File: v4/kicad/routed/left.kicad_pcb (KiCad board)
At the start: 2 copper layers, 158 x 119 mm, 68 parts

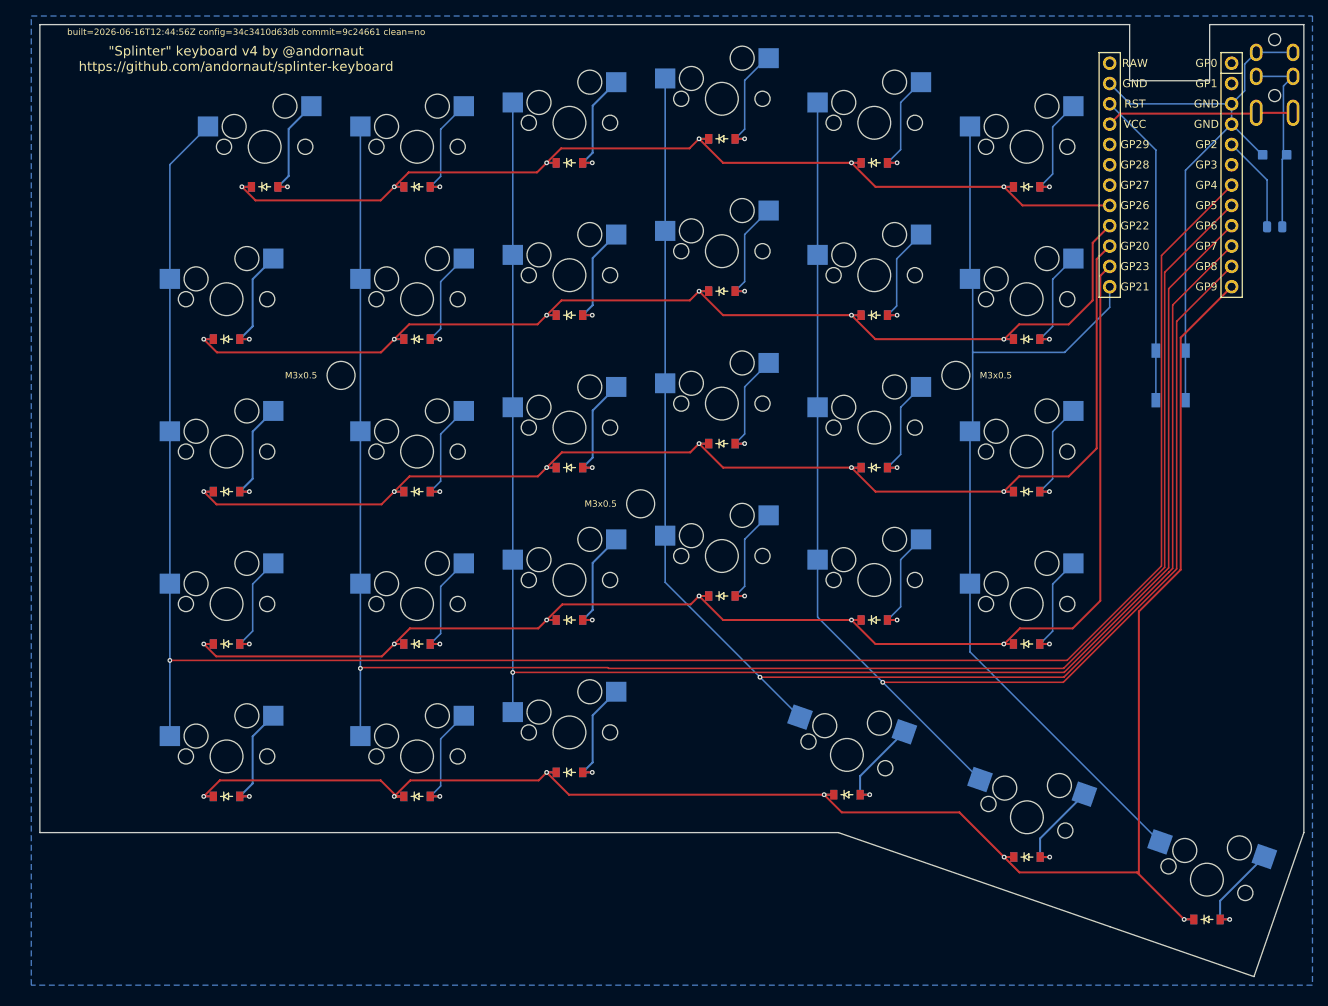
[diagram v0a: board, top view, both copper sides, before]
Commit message: v4: reassign left-half matrix pins, re-sync boards, harden GND guard
config.yaml: column five left -> P15 (was P10) and swap the lower/home/
upper row_net assignments (P14/P16/P10). Re-sync routed/ + unrouted/
left and right boards to the new config.

add-gnd-zone.py: exclude teardrop zones from the already-poured guard (a
teardrop on a GND track is itself a GND zone, which made the guard see a
pour that was never flooded and skip the real fill); clearer
UNCHANGED/ADDED logging.
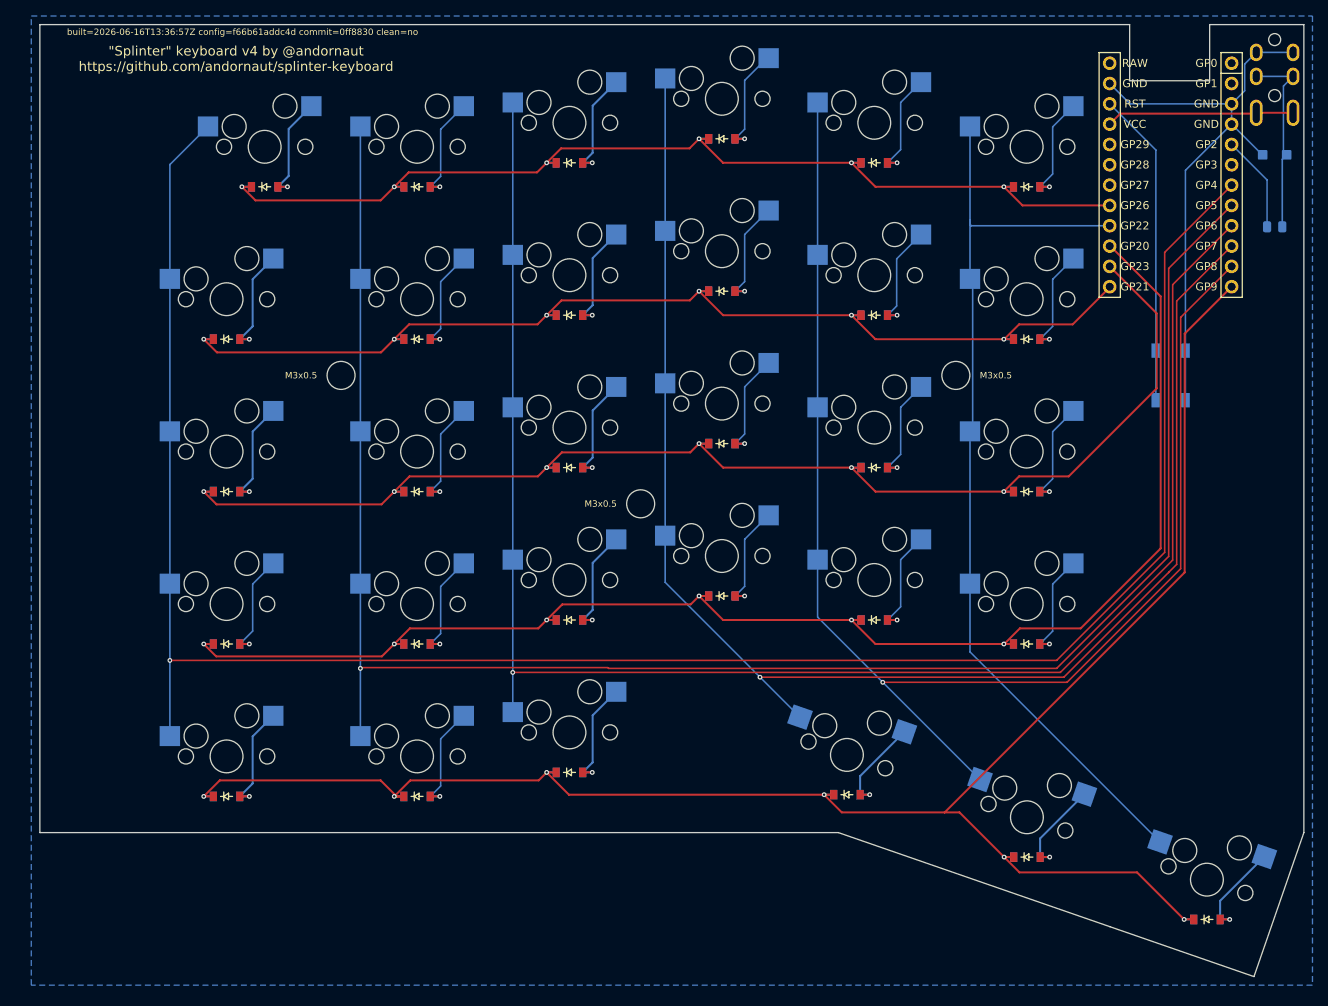
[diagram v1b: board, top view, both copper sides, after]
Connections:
- D12 pad 1: P16 -> P14
- D13 pad 1: P14 -> P16
- D14 pad 1: P15 -> P10
- D16 pad 1: P16 -> P14
- D17 pad 1: P14 -> P16
- D18 pad 1: P15 -> P10
- D2 pad 1: P16 -> P14
- D20 pad 1: P16 -> P14
- D21 pad 1: P14 -> P16
- D22 pad 1: P15 -> P10
- D24 pad 1: P16 -> P14
- D25 pad 1: P14 -> P16
- D26 pad 1: P15 -> P10
- D3 pad 1: P14 -> P16
- D4 pad 1: P15 -> P10
- D7 pad 1: P16 -> P14
- D8 pad 1: P14 -> P16
- D9 pad 1: P15 -> P10
- S24 pad 1: P10 -> P15
- S25 pad 1: P10 -> P15
- S26 pad 1: P10 -> P15
- S27 pad 1: P10 -> P15
- S30 pad 1: P10 -> P15
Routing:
- net P15: track 144.1 -> 116.6 mm, vias 6 -> 0
- net P14: track 160.5 -> 185.6 mm
- net P10: track 120.6 -> 136.7 mm, vias 0 -> 6
- net P16: track 177.2 -> 162.8 mm
- net P9: track 227.2 -> 229.5 mm
- net P4: track 258.2 -> 257.4 mm
- net P5: track 230.8 -> 230.2 mm
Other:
- board text added: "built=2026-06-16T13:36:57Z config=f66b61addc4d commit=0ff8830 clean=no"
- board text removed: "built=2026-06-16T12:44:56Z config=34c3410d63db commit=9c24661 clean=no"

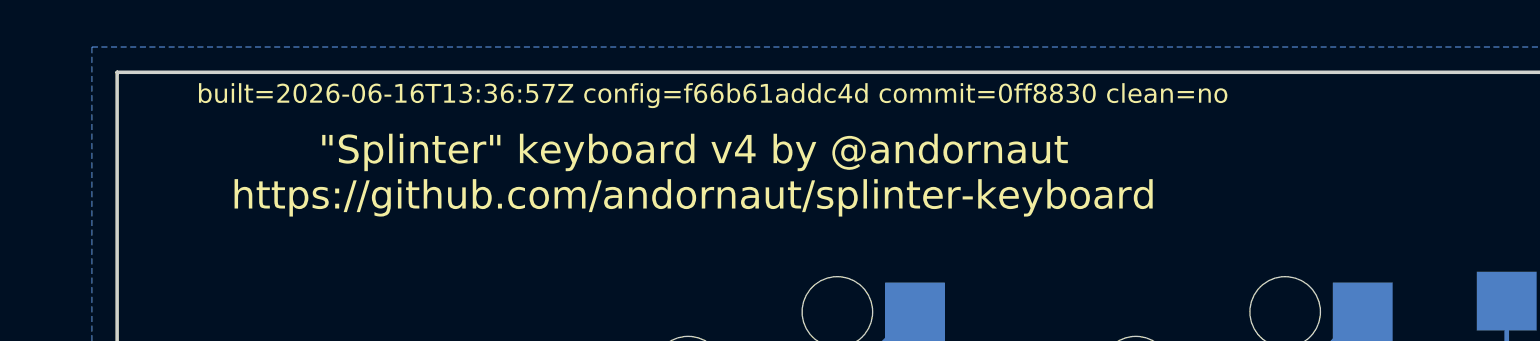
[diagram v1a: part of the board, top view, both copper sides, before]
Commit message: v4: regenerate boards with GND pour fix (JLCPCB order build)
Re-synced unrouted + routed left/right boards. This is the build sent to
JLCPCB: stamp built=2026-06-16T14:04:40Z config=f66b61addc4d commit=44bb610
clean=yes.
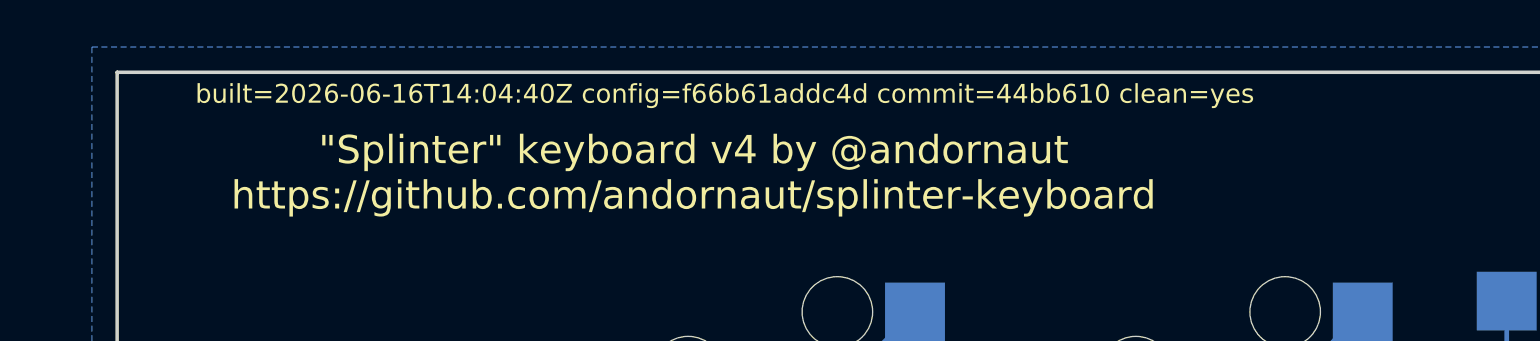
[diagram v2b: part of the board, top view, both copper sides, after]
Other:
- board text added: "built=2026-06-16T14:04:40Z config=f66b61addc4d commit=44bb610 clean=yes"
- board text removed: "built=2026-06-16T13:36:57Z config=f66b61addc4d commit=0ff8830 clean=no"

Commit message: v4: restore right-half teardrops on routed + unrouted masters
The right master carried only 20 teardrop zones (the teardrop-loss
failure that shipped on the first JLCPCB order); re-teardropped to 502,
now symmetric with the left half (464). Tracks, vias, and arcs are
unchanged on both halves (408/70/128 right, 384/65/120 left); the rest
of the diff is KiCad re-save churn. Clears the validate:fab
teardrop-consistency gate.
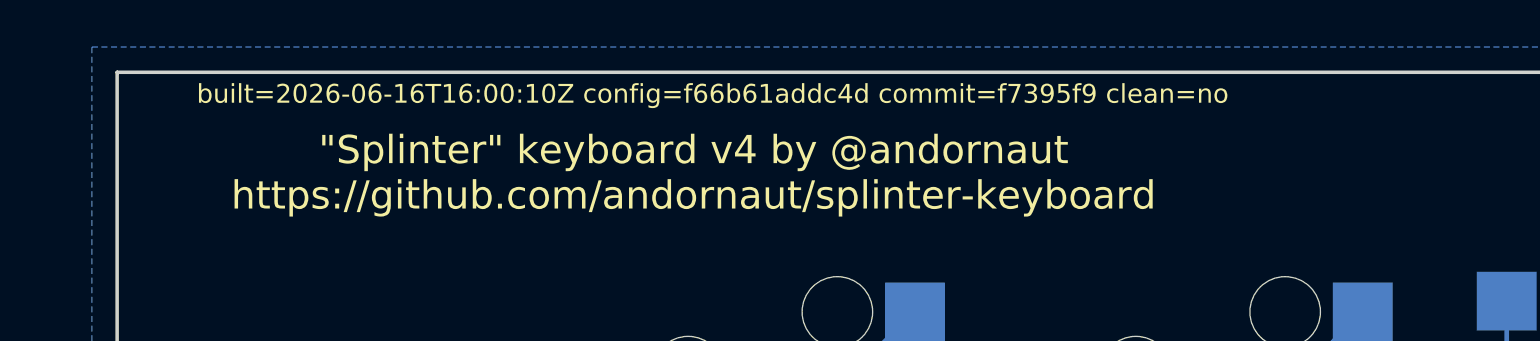
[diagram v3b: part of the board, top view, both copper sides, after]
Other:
- board text added: "built=2026-06-16T16:00:10Z config=f66b61addc4d commit=f7395f9 clean=no"
- board text removed: "built=2026-06-16T14:04:40Z config=f66b61addc4d commit=44bb610 clean=yes"

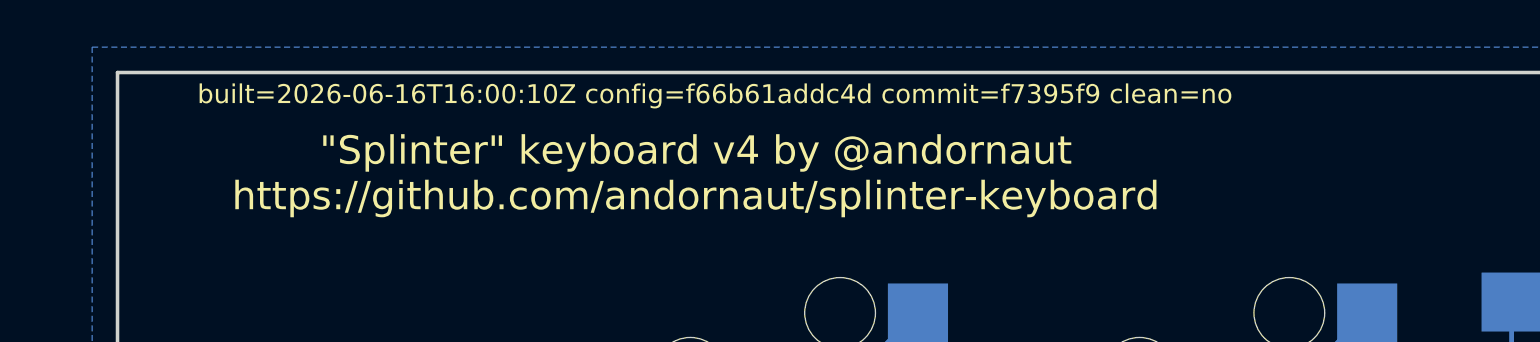
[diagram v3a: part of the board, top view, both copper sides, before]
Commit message: v4: fabrication build (ordering this from JLCPCB)
Validated fab-ready and sent to JLCPCB. Teardrops symmetric (459 left /
496 right zones), GND pour filled on B.Cu (~13000mm^2 master, ~157x118mm
flood in the shipped B_Cu gerber), DRC clean (0 violations / 0 unconnected
both halves), provenance matches config, gerber set + assembly complete.

Provenance stamp (routed masters):
  splinter v=v4 built=2026-06-16T16:30:02Z config=f66b61addc4d commit=d2fd01a clean=yes
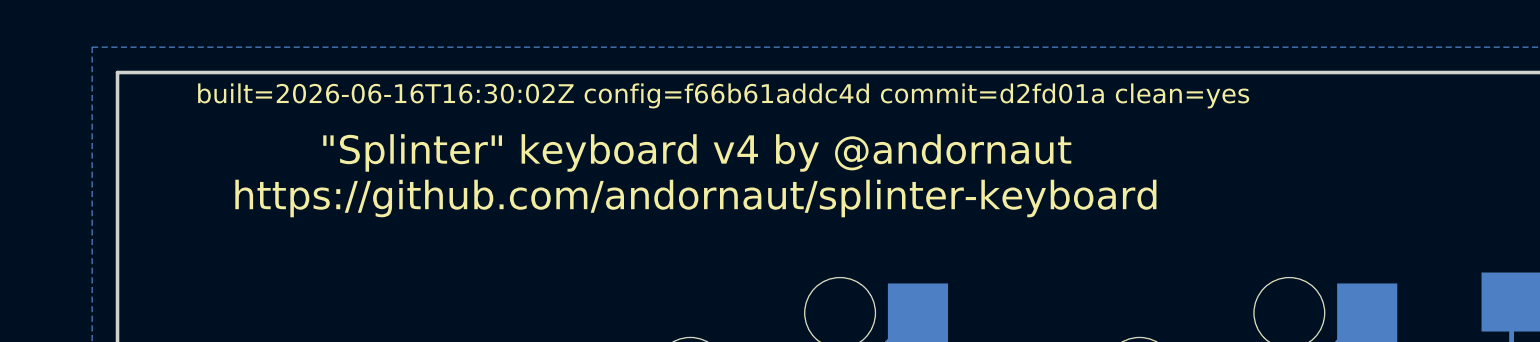
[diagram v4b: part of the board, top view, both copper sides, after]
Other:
- board text added: "built=2026-06-16T16:30:02Z config=f66b61addc4d commit=d2fd01a clean=yes"
- board text removed: "built=2026-06-16T16:00:10Z config=f66b61addc4d commit=f7395f9 clean=no"

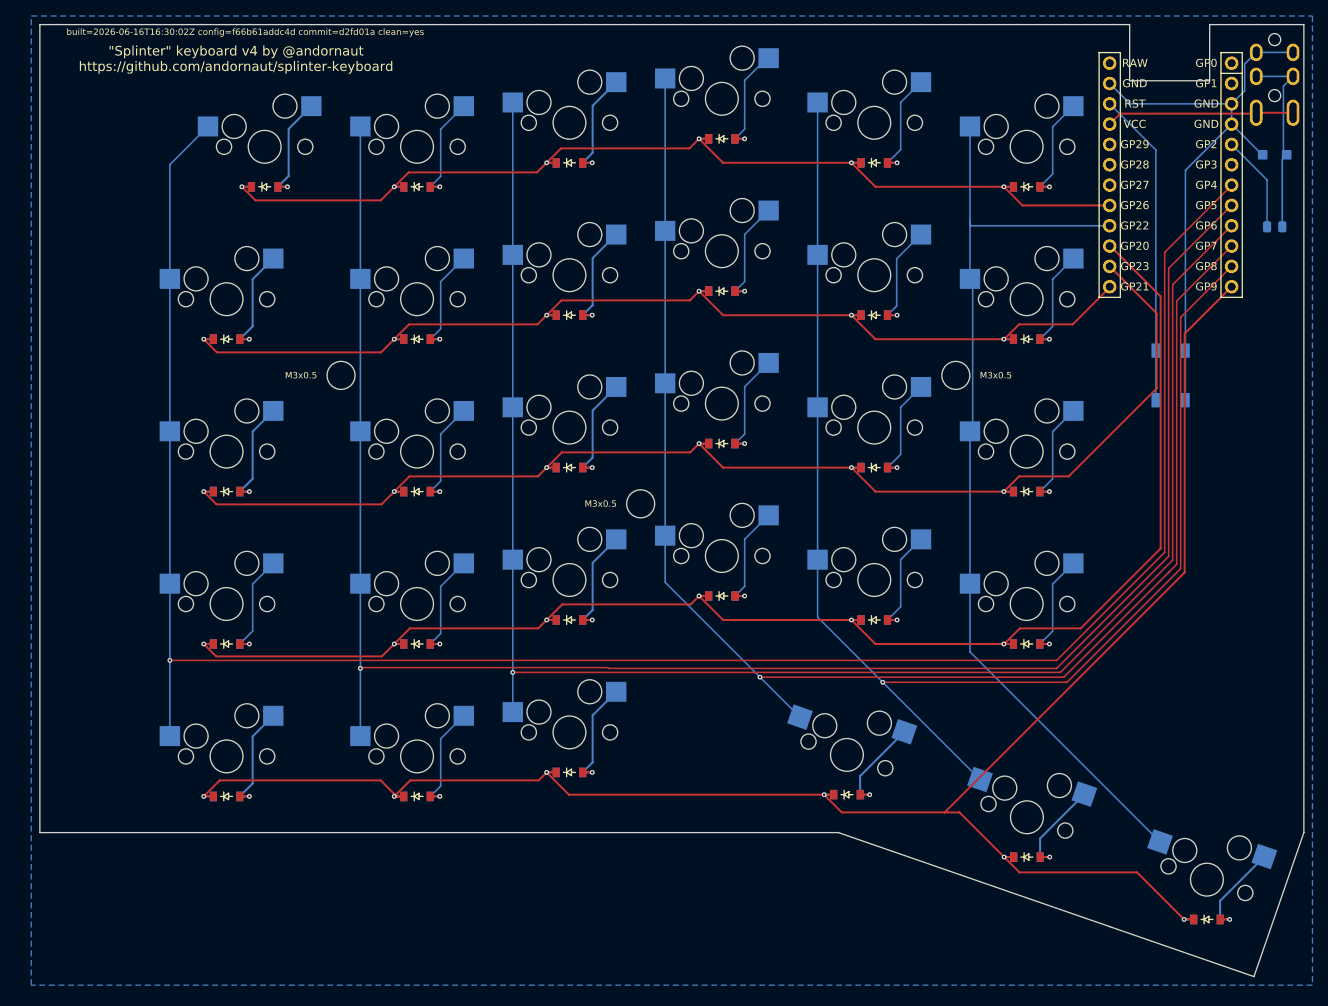
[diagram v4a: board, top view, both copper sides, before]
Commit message: v4: square-cornered USB-C notch, unified 0.25mm clearance, onshape case notes
- config: subtract the USB-C cutout (_usbleft/_usbright) after the exterior
  fillet so the notch keeps square corners; tie it to mcu_reset_x so it tracks
  the MCU. Nudge MCU/reset/TRRS/TVS/resistor placement.
- apply-project-settings: add ensure_default_clearance so the Default net class
  clearance is 0.25mm, unifying the gap with VCC across the board.
- regenerate routed + unrouted boards and project files.
- onshape: add v4 case design guidance (FDM + JLCCNC sandwich topology).
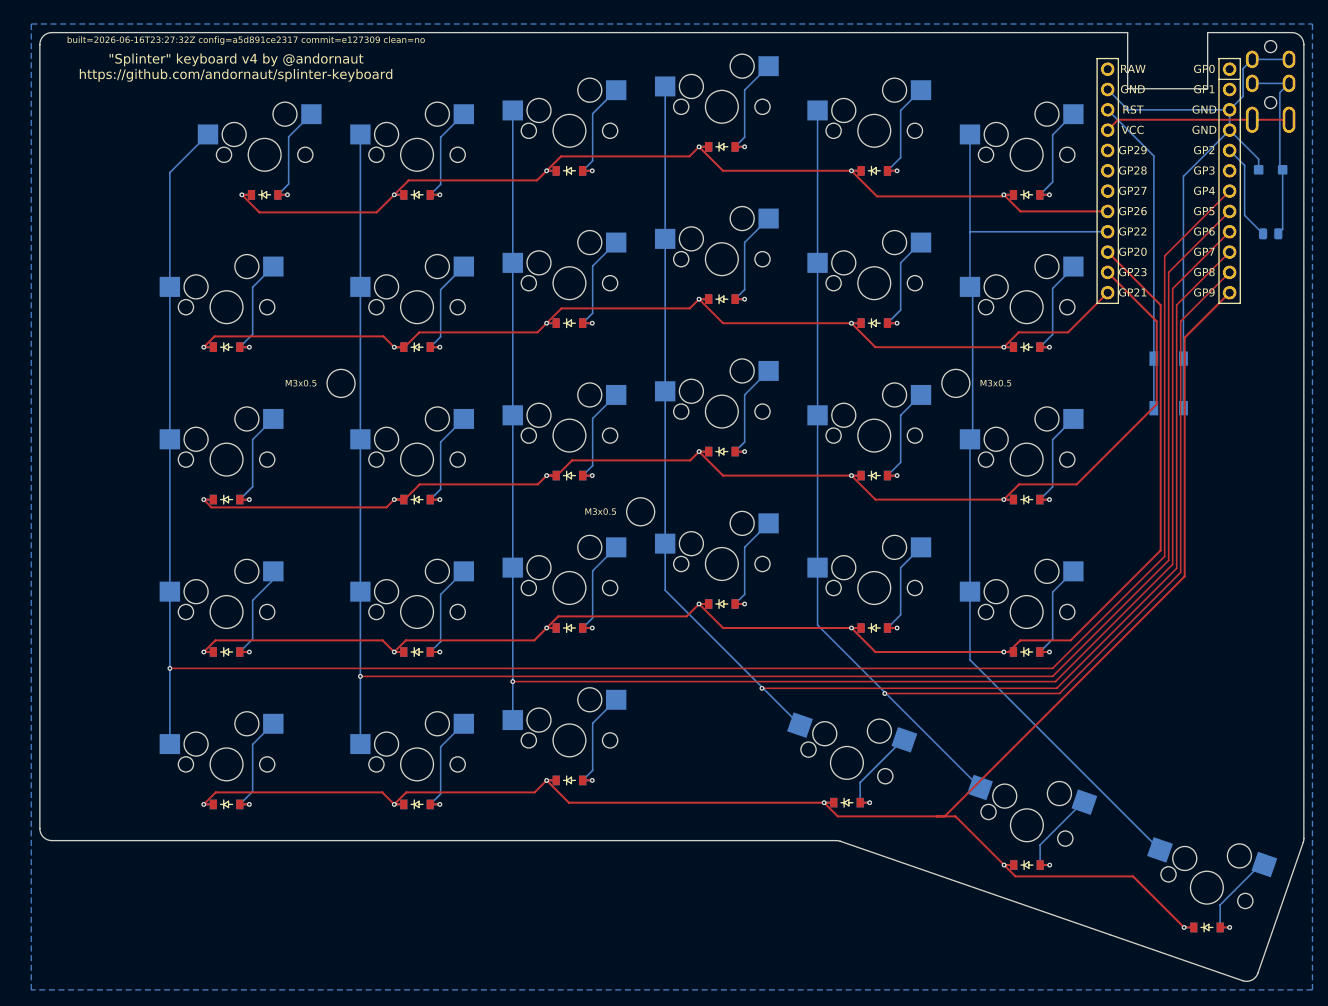
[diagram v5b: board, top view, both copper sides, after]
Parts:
- moved D31 1.94 mm to (284.8, 106.7)
- moved B1 1.03 mm to (272.0, 133.4)
- moved R1 1.01 mm to (284.8, 114.7)
- moved TRRS1 1.01 mm to (284.8, 89.7)
- moved D1 1.00 mm to (154.2, 186.0)
- moved D10 1.00 mm to (178.1, 109.8)
- moved D11 1.00 mm to (197.1, 183.0)
- moved D12 1.00 mm to (197.1, 163.9)
- moved D13 1.00 mm to (197.1, 144.9)
- moved D14 1.00 mm to (197.1, 125.8)
- moved D15 1.00 mm to (197.1, 106.8)
- moved D16 1.00 mm to (216.2, 160.9)
- moved D17 1.00 mm to (216.2, 141.9)
- moved D18 1.00 mm to (216.2, 122.8)
- moved D19 1.00 mm to (216.2, 103.8)
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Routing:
- net P9: track 229.5 -> 228.3 mm
- net GND: track 73.4 -> 74.5 mm
- net zero_lower: track 14.2 -> 13.2 mm
- net P15: track 116.6 -> 115.8 mm
- net P14: track 185.6 -> 184.9 mm
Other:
- board size 158 x 119 mm -> 158 x 118.6 mm
- board text added: "built=2026-06-16T23:27:32Z config=a5d891ce2317 commit=e127309 clean=no"
- board text removed: "built=2026-06-16T16:30:02Z config=f66b61addc4d commit=d2fd01a clean=yes"

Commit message: v4: rebuild boards, restamp provenance clean=yes at fbbf6c4
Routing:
- net P14: track 184.9 -> 186.1 mm
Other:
- board text added: "built=2026-06-17T00:36:15Z config=a5d891ce2317 commit=fbbf6c4 clean=yes"
- board text removed: "built=2026-06-16T23:27:32Z config=a5d891ce2317 commit=e127309 clean=no"
